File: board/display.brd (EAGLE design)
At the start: 160 x 100 mm, 39 parts, among them IC1 MEGA8-P, IC2 74HCT595N, IC3 7805T, Q1 8MHz, Q2 MMBT4403LT1SMD, Q3 MMBT4403LT1SMD, Q4 MMBT4403LT1SMD, Q5 MMBT4403LT1SMD, X1 MKDSN1,5/2-5,08

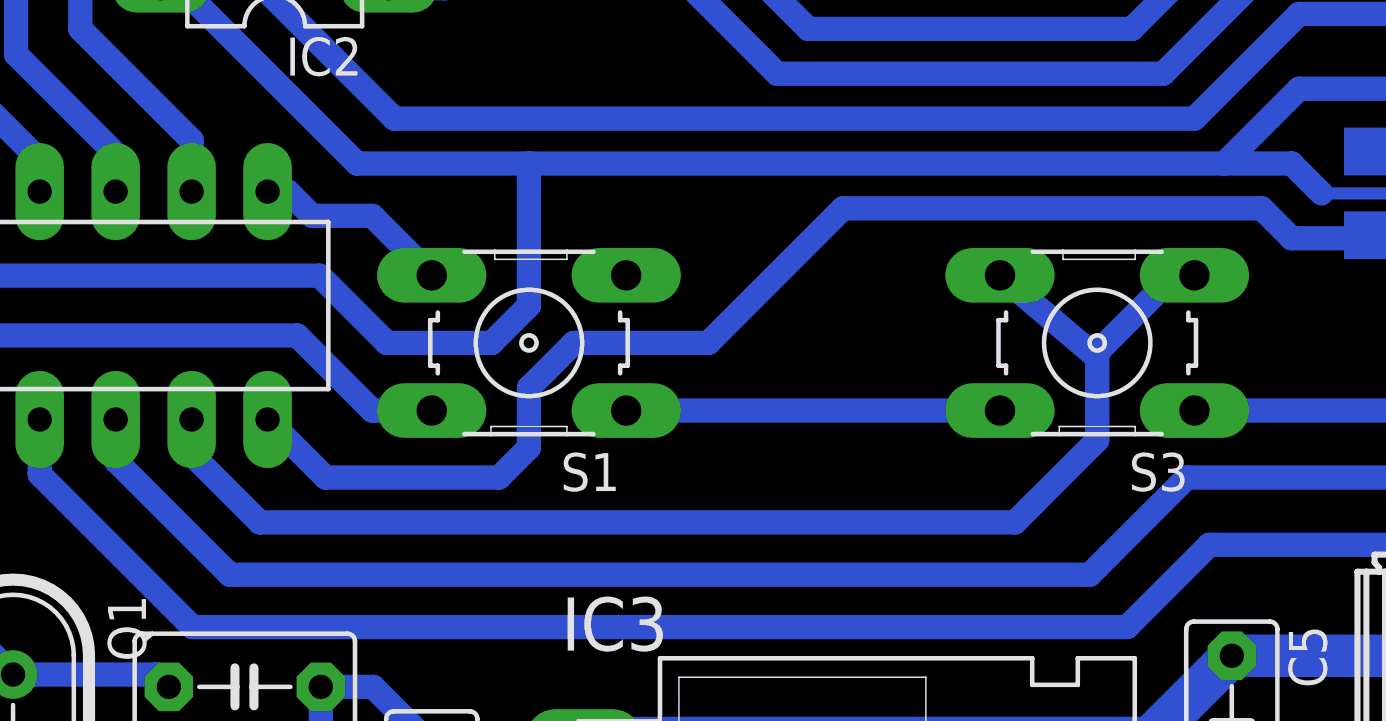
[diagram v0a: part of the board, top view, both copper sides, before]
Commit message: working buttons and set temperature
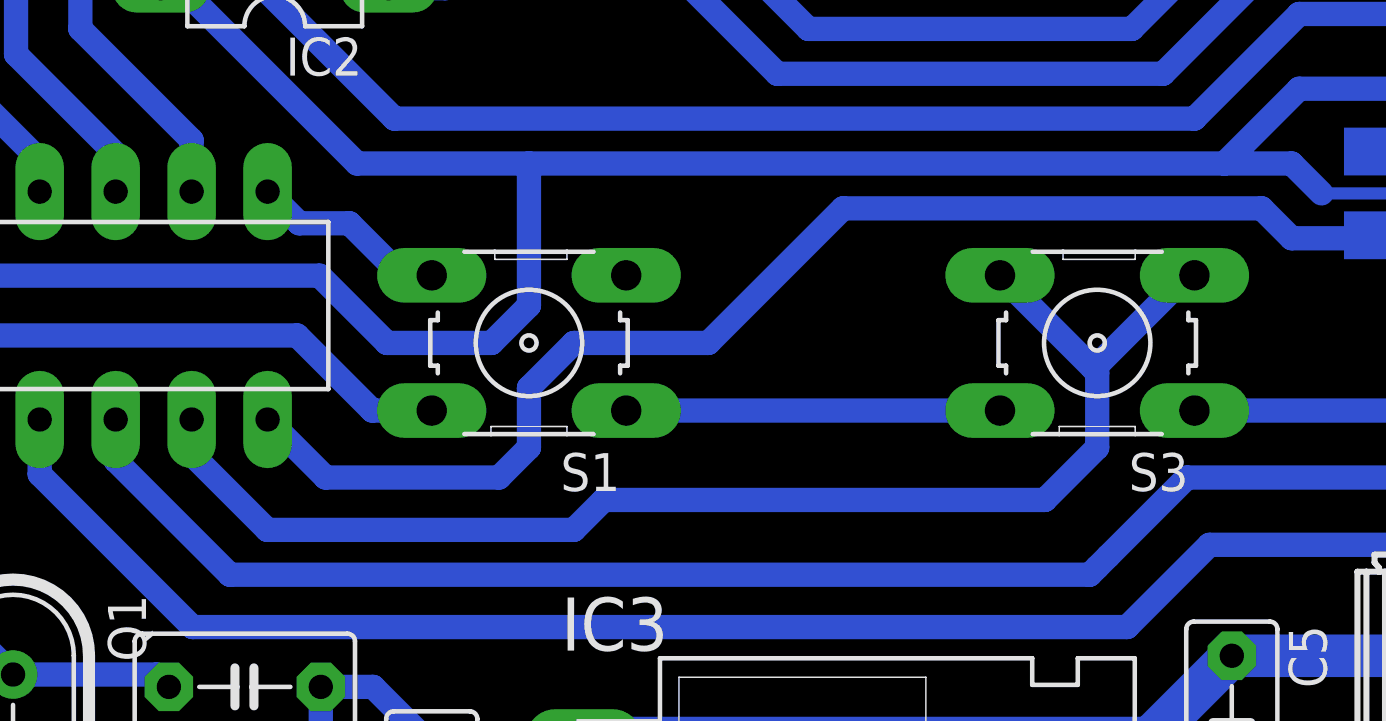
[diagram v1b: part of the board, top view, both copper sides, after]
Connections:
- net SW_ENTER: now also IC1.15, S1.3, S1.4; no longer IC1.13, S3.3, S3.4
- net SW_UP: now also IC1.13, S3.3, S3.4; no longer IC1.15, S1.3, S1.4
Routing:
- net SW_UP: track 6.65 -> 45.4 mm
- net SW_ENTER: track 45.0 -> 6.65 mm
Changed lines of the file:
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@@
 <wire x1="27.4" y1="19.55" x2="26.25" y2="18.4" width="0.8128" layer="16"/>
-</signal>
-<signal name="SW_UP">
-<contactref element="S1" pad="3"/>
-<contactref element="S1" pad="4"/>
-<contactref element="IC1" pad="15"/>
-<wire x1="50.26" y1="29.81" x2="50.94" y2="29.81" width="0.8128" layer="16"/>
-<wire x1="50.94" y1="29.81" x2="51.75" y2="29" width="0.8128" layer="16"/>
-<wire x1="51.75" y1="29" x2="53.7594" y2="29" width="0.8128" layer="16"/>
-<wire x1="53.7594" y1="29" x2="55.7488" y2="27.0106" width="0.8128" layer="16"/>
-<wire x1="55.7488" y1="27.0106" x2="62.2512" y2="27.0106" width="0" layer="19" extent="1-1"/>
 </signal>
 <signal name="SW_DOWN">
@@
 <wire x1="81.75" y1="18" x2="79" y2="15.25" width="0.8128" layer="16"/>
 <wire x1="100.7512" y1="27.0106" x2="94.2488" y2="27.0106" width="0" layer="19" extent="1-1"/>
-</signal>
-<signal name="SW_ENTER">
-<contactref element="S3" pad="3"/>
-<contactref element="S3" pad="4"/>
-<contactref element="IC1" pad="13"/>
-<wire x1="75.75" y1="19.25" x2="75.875" y2="19.375" width="0.8128" layer="16"/>
-<wire x1="75.875" y1="19.375" x2="78" y2="21.5" width="0.8128" layer="16"/>
-<wire x1="78" y1="21.5" x2="78" y2="24.2594" width="0.8128" layer="16"/>
-<wire x1="78" y1="24.2594" x2="77.9037625" y2="24.3408375" width="0.8128" layer="16"/>
-<wire x1="77.9037625" y1="24.3408375" x2="74.7488" y2="27.0106" width="0.8128" layer="16"/>
-<wire x1="50" y1="18.75" x2="47.72" y2="21.03" width="0.8128" layer="16"/>
-<wire x1="47.72" y1="21.03" x2="47.72" y2="22.19" width="0.8128" layer="16"/>
-<wire x1="81.2512" y1="27.0106" x2="80.573525" y2="27.0106" width="0.8128" layer="16"/>
-<wire x1="80.573525" y1="27.0106" x2="77.9037625" y2="24.3408375" width="0.8128" layer="16"/>
-<wire x1="50" y1="18.75" x2="75.25" y2="18.75" width="0.8128" layer="16"/>
-<wire x1="75.25" y1="18.75" x2="75.75" y2="19.25" width="0.8128" layer="16"/>
 </signal>
 <signal name="N$3">
@@
 <wire x1="21.29" y1="33.04" x2="21.29" y2="35.25" width="0.8128" layer="16"/>
 </signal>
+<signal name="SW_ENTER">
+<contactref element="IC1" pad="15"/>
+<contactref element="S1" pad="3"/>
+<contactref element="S1" pad="4"/>
+<wire x1="55.7488" y1="27.0106" x2="62.2512" y2="27.0106" width="0" layer="19" extent="1-1"/>
+<wire x1="55.7488" y1="27.0106" x2="54.7394" y2="27.0106" width="0.8128" layer="16"/>
+<wire x1="54.7394" y1="27.0106" x2="53" y2="28.75" width="0.8128" layer="16"/>
+<wire x1="53" y1="28.75" x2="51.32" y2="28.75" width="0.8128" layer="16"/>
+<wire x1="51.32" y1="28.75" x2="50.26" y2="29.81" width="0.8128" layer="16"/>
+</signal>
+<signal name="SW_UP">
+<contactref element="S3" pad="3"/>
+<contactref element="S3" pad="4"/>
+<contactref element="IC1" pad="13"/>
+<wire x1="47.72" y1="22.19" x2="47.72" y2="21.03" width="0.8128" layer="16"/>
+<wire x1="47.72" y1="21.03" x2="50.25" y2="18.5" width="0.8128" layer="16"/>
+<wire x1="50.25" y1="18.5" x2="60.5" y2="18.5" width="0.8128" layer="16"/>
+<wire x1="60.5" y1="18.5" x2="61.5" y2="19.5" width="0.8128" layer="16"/>
+<wire x1="61.5" y1="19.5" x2="76.25" y2="19.5" width="0.8128" layer="16"/>
+<wire x1="76.25" y1="19.5" x2="78" y2="21.25" width="0.8128" layer="16"/>
+<wire x1="78" y1="21.25" x2="78" y2="23.7594" width="0.8128" layer="16"/>
+<wire x1="78" y1="23.7594" x2="77.8797" y2="23.8797" width="0.8128" layer="16"/>
+<wire x1="77.8797" y1="23.8797" x2="74.7488" y2="27.0106" width="0.8128" layer="16"/>
+<wire x1="81.2512" y1="27.0106" x2="81.0106" y2="27.0106" width="0.8128" layer="16"/>
+<wire x1="81.0106" y1="27.0106" x2="77.8797" y2="23.8797" width="0.8128" layer="16"/>
+</signal>
 </signals>
